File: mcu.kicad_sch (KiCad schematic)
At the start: 8 parts, among them J10 LOLIN-S3 (R), J11 ESP32-S3-DEVKITC-1 (L), J12 ESP32-S3-DEVKITC-1 (R), J13 LOLIN-S2-MINI (L Outer), J14 LOLIN-S2-MINI (R Outer), J15 LOLIN-S2-MINI (L Inner), J16 LOLIN-S2-MINI (R Inner), J9 LOLIN-S3 (L)

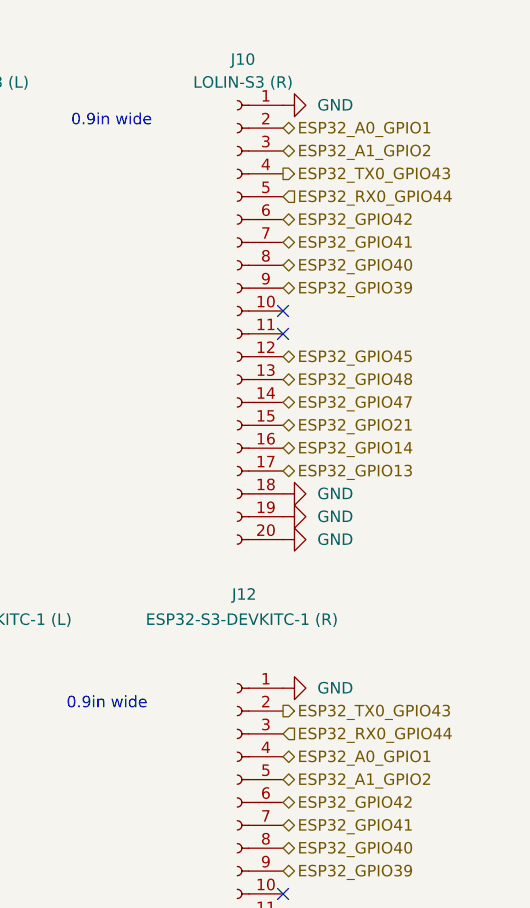
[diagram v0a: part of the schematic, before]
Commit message: Rename UART pins to use Espressif convention
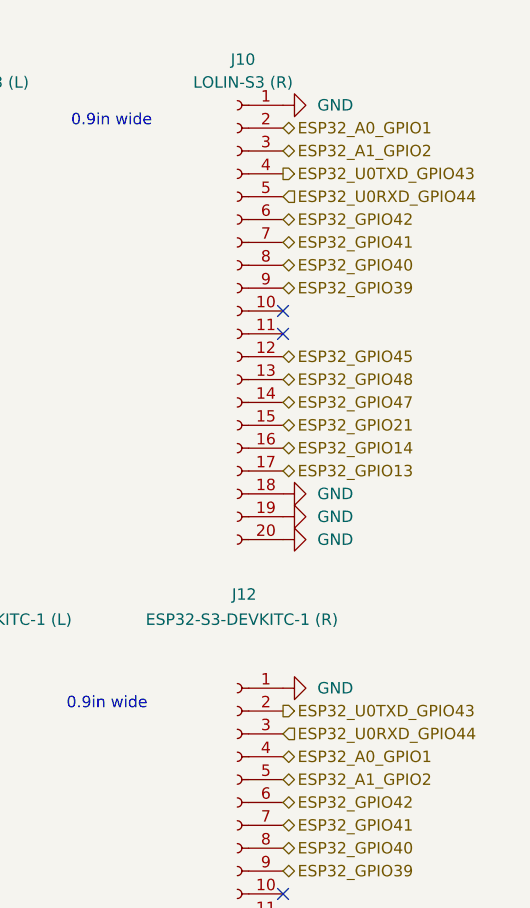
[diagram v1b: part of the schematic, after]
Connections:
- net ESP32_RX0_GPIO44 renamed ESP32_U0RXD_GPIO44
- net ESP32_TX0_GPIO43 renamed ESP32_U0TXD_GPIO43
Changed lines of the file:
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@@
 		)
 	)
-	(hierarchical_label "ESP32_RX0_GPIO44"
+	(hierarchical_label "ESP32_U0RXD_GPIO44"
 		(shape input)
 		(at 69.85 86.36 0)
@@
 		)
 	)
-	(hierarchical_label "ESP32_TX0_GPIO43"
+	(hierarchical_label "ESP32_U0TXD_GPIO43"
 		(shape output)
 		(at 69.85 83.82 0)
@@
 		)
 	)
-	(hierarchical_label "ESP32_TX0_GPIO43"
+	(hierarchical_label "ESP32_U0TXD_GPIO43"
 		(shape output)
 		(at 69.85 24.13 0)
@@
 		)
 	)
-	(hierarchical_label "ESP32_RX0_GPIO44"
+	(hierarchical_label "ESP32_U0RXD_GPIO44"
 		(shape input)
 		(at 69.85 26.67 0)

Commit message: Assign footprints for the remaining components
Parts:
- J10, J9: footprint (none) -> Connector_PinSocket_2.54mm:PinSocket_1x20_P2.54mm_Vertical
- J11, J12: footprint (none) -> Connector_PinHeader_2.54mm:PinHeader_1x22_P2.54mm_Vertical
- J13, J14, J15, J16: footprint (none) -> Connector_PinHeader_2.54mm:PinHeader_1x08_P2.54mm_Vertical
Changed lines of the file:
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@@
 			)
 		)
-		(property "Footprint" ""
+		(property "Footprint" "Connector_PinHeader_2.54mm:PinHeader_1x08_P2.54mm_Vertical"
 			(at 64.77 181.61 0)
 			(effects
@@
 			)
 		)
-		(property "Footprint" ""
+		(property "Footprint" "Connector_PinSocket_2.54mm:PinSocket_1x20_P2.54mm_Vertical"
 			(at 64.77 39.37 0)
 			(effects
@@
 			)
 		)
-		(property "Footprint" ""
+		(property "Footprint" "Connector_PinSocket_2.54mm:PinSocket_1x20_P2.54mm_Vertical"
 			(at 36.83 39.37 0)
 			(effects
@@
 			)
 		)
-		(property "Footprint" ""
+		(property "Footprint" "Connector_PinHeader_2.54mm:PinHeader_1x08_P2.54mm_Vertical"
 			(at 36.83 181.61 0)
 			(effects
@@
 			)
 		)
-		(property "Footprint" ""
+		(property "Footprint" "Connector_PinHeader_2.54mm:PinHeader_1x08_P2.54mm_Vertical"
 			(at 67.31 153.67 0)
 			(effects
@@
 			)
 		)
-		(property "Footprint" ""
+		(property "Footprint" "Connector_PinHeader_2.54mm:PinHeader_1x08_P2.54mm_Vertical"
 			(at 34.29 153.67 0)
 			(effects
@@
 			)
 		)
-		(property "Footprint" ""
+		(property "Footprint" "Connector_PinHeader_2.54mm:PinHeader_1x22_P2.54mm_Vertical"
 			(at 64.77 106.68 0)
 			(effects
@@
 			)
 		)
-		(property "Footprint" ""
+		(property "Footprint" "Connector_PinHeader_2.54mm:PinHeader_1x22_P2.54mm_Vertical"
 			(at 36.83 106.68 0)
 			(effects

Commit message: Place all components
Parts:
- removed J13: LOLIN-S2-MINI (L Outer), Connector_PinHeader_2.54mm:PinHeader_1x08_P2.54mm_Vertical, symbol Connector:Conn_01x08_Socket
- removed J14: LOLIN-S2-MINI (R Outer), Connector_PinHeader_2.54mm:PinHeader_1x08_P2.54mm_Vertical, symbol Connector:Conn_01x08_Socket
- removed J15: LOLIN-S2-MINI (L Inner), Connector_PinHeader_2.54mm:PinHeader_1x08_P2.54mm_Vertical, symbol Connector:Conn_01x08_Socket
- removed J16: LOLIN-S2-MINI (R Inner), Connector_PinHeader_2.54mm:PinHeader_1x08_P2.54mm_Vertical, symbol Connector:Conn_01x08_Socket
- added J13: LOLIN-S2-MINI (L), Connector_PinSocket_2.54mm:PinSocket_2x08_P2.54mm_Vertical, symbol Connector_Generic:Conn_02x08_Odd_Even
- added J14: LOLIN-S2-MINI (R), Connector_PinSocket_2.54mm:PinSocket_2x08_P2.54mm_Vertical, symbol Connector_Generic:Conn_02x08_Odd_Even
- J11, J12: footprint Connector_PinHeader_2.54mm:PinHeader_1x22_P2.54mm_Vertical -> Connector_PinSocket_2.54mm:PinSocket_1x22_P2.54mm_Vertical
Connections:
- net +3.3V: now also J13.16 (Pin_16)
- net +5V: now also J14.15 (Pin_15)
- net ESP32_A0_GPIO1: now also J13.1 (Pin_1)
- net ESP32_A1_GPIO2: now also J13.3 (Pin_3)
- net ESP32_A2_GPIO3: now also J13.4 (Pin_4)
- net ESP32_A3_GPIO4: now also J13.5 (Pin_5)
- net ESP32_A4_GPIO5: now also J13.6 (Pin_6)
- net ESP32_A5_GPIO6: now also J13.7 (Pin_7)
- net ESP32_A6_GPIO7: now also J13.8 (Pin_8)
- net ESP32_A7_GPIO8: now also J13.9 (Pin_9)
- net ESP32_A8_GPIO9: now also J13.10 (Pin_10)
- net ESP32_A9_GPIO10: now also J13.11 (Pin_11)
- net ESP32_GPIO11: now also J13.12 (Pin_12)
- net ESP32_GPIO12: now also J13.14 (Pin_14)
- net ESP32_GPIO13: now also J13.13 (Pin_13)
- net ESP32_GPIO14: now also J13.15 (Pin_15)
- net ESP32_GPIO16: now also J14.11 (Pin_11)
- net ESP32_GPIO17: now also J14.12 (Pin_12)
- net ESP32_GPIO18: now also J14.9 (Pin_9)
- net ESP32_GPIO21: now also J14.10 (Pin_10)
- net ESP32_GPIO33: now also J14.7 (Pin_7)
- net ESP32_GPIO34: now also J14.8 (Pin_8)
- net ESP32_GPIO35: now also J14.5 (Pin_5)
- net ESP32_GPIO36: now also J14.6 (Pin_6)
- net ESP32_GPIO37: now also J14.3 (Pin_3)
- net ESP32_GPIO38: now also J14.4 (Pin_4)
- net ESP32_GPIO39: now also J14.1 (Pin_1)
- net ESP32_GPIO40: now also J14.2 (Pin_2)
- net GND: now also J14.13 (Pin_13), J14.14 (Pin_14)
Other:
- note added: "0.9in wide (outer) 0.7in wide (inner)"
- note removed: "0.7in wide"
- moved on the sheet: J10, J11, J12, J9

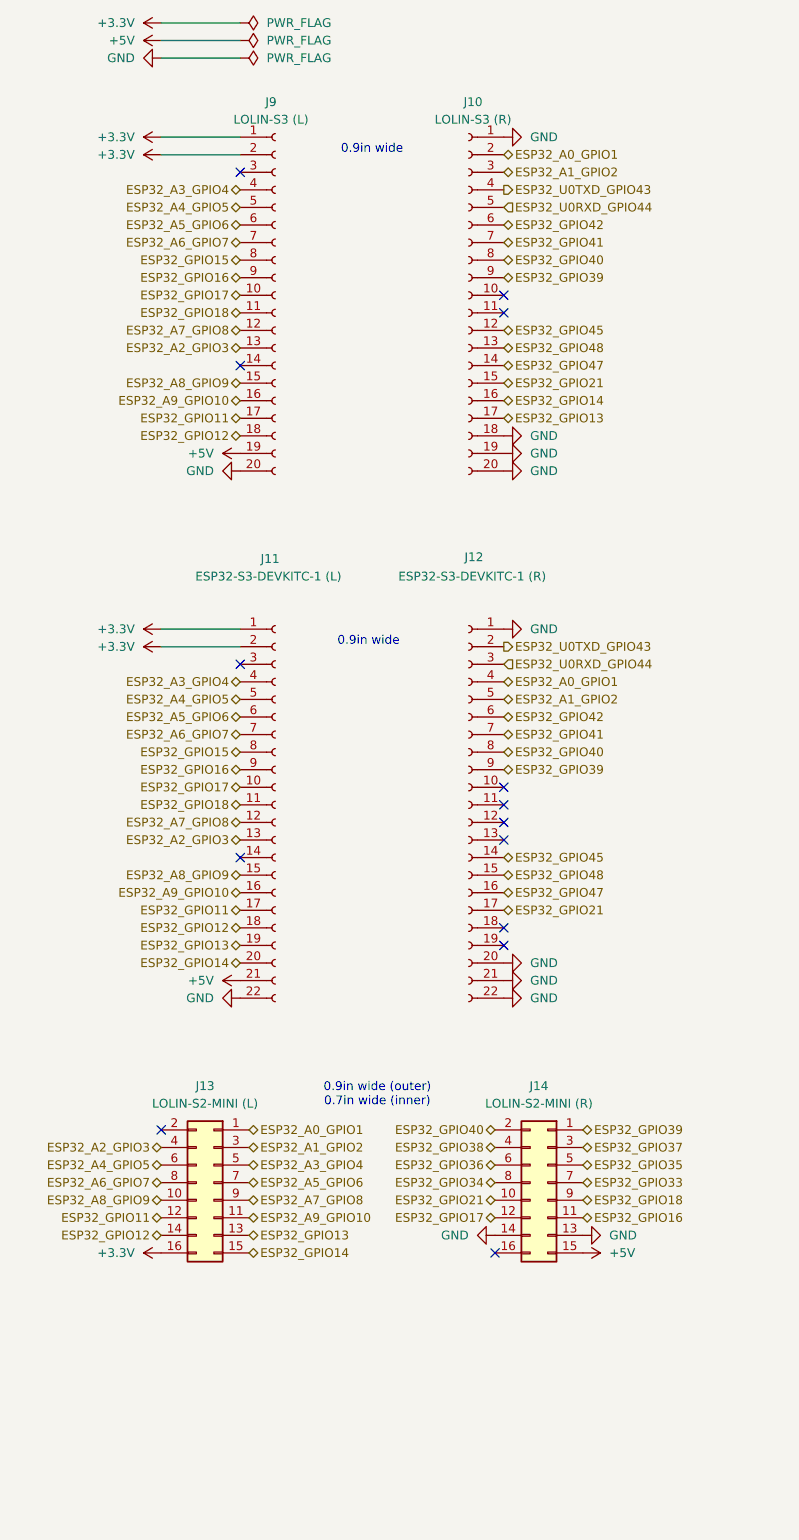
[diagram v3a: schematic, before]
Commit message: Add LOLIN S3 mini support
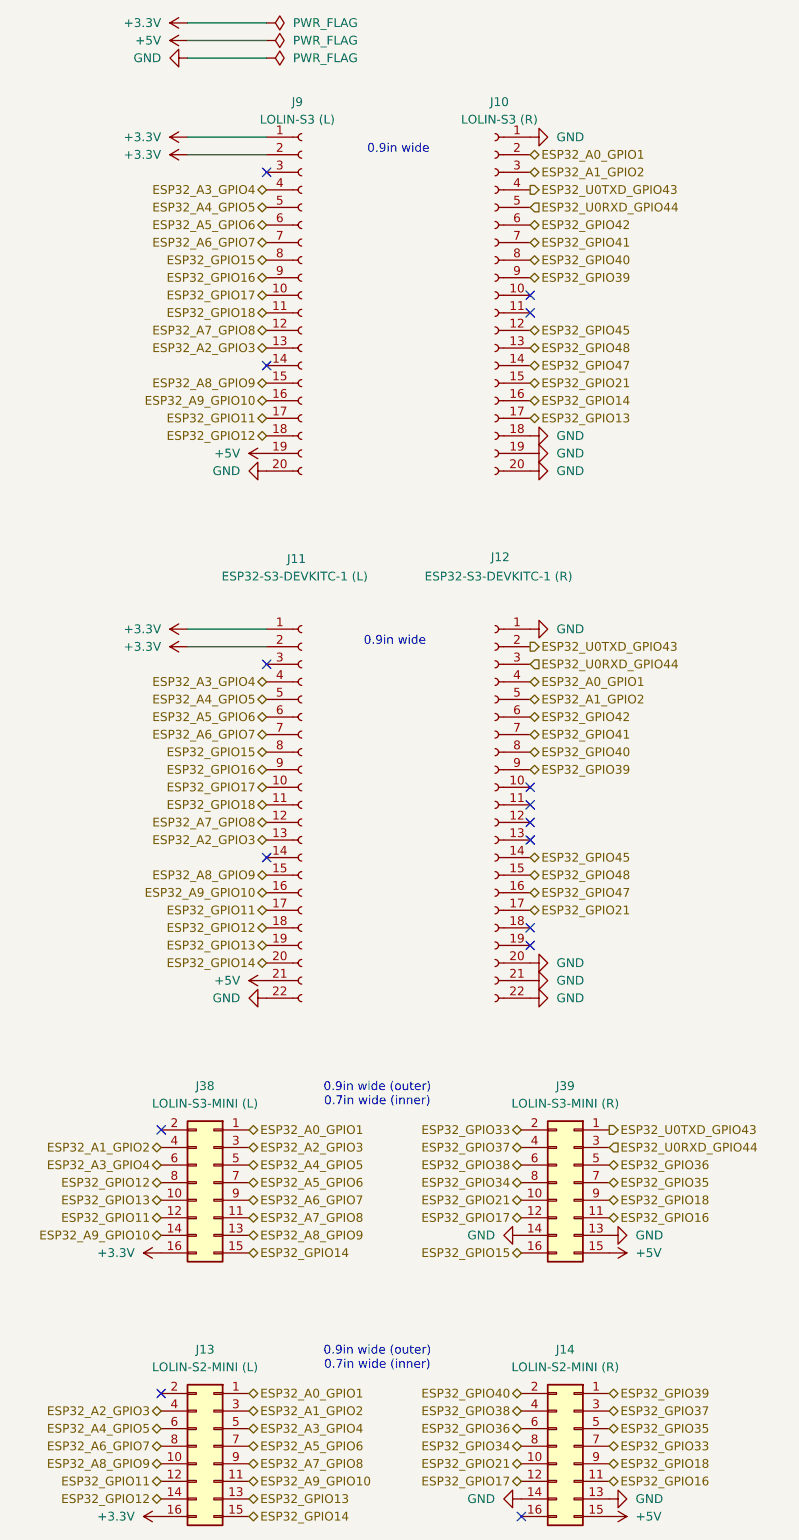
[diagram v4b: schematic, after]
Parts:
- added J13: LOLIN-S2-MINI (L), Connector_PinSocket_2.54mm:PinSocket_2x08_P2.54mm_Vertical, symbol Connector_Generic:Conn_02x08_Odd_Even
- added J14: LOLIN-S2-MINI (R), Connector_PinSocket_2.54mm:PinSocket_2x08_P2.54mm_Vertical, symbol Connector_Generic:Conn_02x08_Odd_Even
- J38: renamed from J13; value LOLIN-S2-MINI (L) -> LOLIN-S3-MINI (L)
- J39: renamed from J14; value LOLIN-S2-MINI (R) -> LOLIN-S3-MINI (R)
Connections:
- net +3.3V: now also J13.16 (Pin_16)
- net +5V: now also J14.15 (Pin_15)
- net ESP32_A0_GPIO1: now also J13.1 (Pin_1)
- net ESP32_A1_GPIO2: now also J38.4 (Pin_4), J13.3 (Pin_3); no longer J38.3 (Pin_3)
- net ESP32_A2_GPIO3: now also J38.3 (Pin_3), J13.4 (Pin_4); no longer J38.4 (Pin_4)
- net ESP32_A3_GPIO4: now also J38.6 (Pin_6), J13.5 (Pin_5); no longer J38.5 (Pin_5)
- net ESP32_A4_GPIO5: now also J38.5 (Pin_5), J13.6 (Pin_6); no longer J38.6 (Pin_6)
- net ESP32_A5_GPIO6: now also J13.7 (Pin_7)
- net ESP32_A6_GPIO7: now also J38.9 (Pin_9), J13.8 (Pin_8); no longer J38.8 (Pin_8)
- net ESP32_A7_GPIO8: now also J38.11 (Pin_11), J13.9 (Pin_9); no longer J38.9 (Pin_9)
- net ESP32_A8_GPIO9: now also J38.13 (Pin_13), J13.10 (Pin_10); no longer J38.10 (Pin_10)
- net ESP32_A9_GPIO10: now also J38.14 (Pin_14), J13.11 (Pin_11); no longer J38.11 (Pin_11)
- net ESP32_GPIO11: now also J13.12 (Pin_12)
- net ESP32_GPIO12: now also J38.8 (Pin_8), J13.14 (Pin_14); no longer J38.14 (Pin_14)
- net ESP32_GPIO13: now also J38.10 (Pin_10), J13.13 (Pin_13); no longer J38.13 (Pin_13)
- net ESP32_GPIO14: now also J13.15 (Pin_15)
- net ESP32_GPIO15: now also J39.16 (Pin_16)
- net ESP32_GPIO16: now also J14.11 (Pin_11)
- net ESP32_GPIO17: now also J14.12 (Pin_12)
- net ESP32_GPIO18: now also J14.9 (Pin_9)
- net ESP32_GPIO21: now also J14.10 (Pin_10)
- net ESP32_GPIO33: now also J39.2 (Pin_2), J14.7 (Pin_7); no longer J39.7 (Pin_7)
- net ESP32_GPIO34: now also J14.8 (Pin_8)
- net ESP32_GPIO35: now also J39.7 (Pin_7), J14.5 (Pin_5); no longer J39.5 (Pin_5)
- net ESP32_GPIO36: now also J39.5 (Pin_5), J14.6 (Pin_6); no longer J39.6 (Pin_6)
- net ESP32_GPIO37: now also J39.4 (Pin_4), J14.3 (Pin_3); no longer J39.3 (Pin_3)
- net ESP32_GPIO38: now also J39.6 (Pin_6), J14.4 (Pin_4); no longer J39.4 (Pin_4)
- net ESP32_GPIO39: now also J14.1 (Pin_1); no longer J39.1 (Pin_1)
- net ESP32_GPIO40: now also J14.2 (Pin_2); no longer J39.2 (Pin_2)
- net ESP32_U0RXD_GPIO44: now also J39.3 (Pin_3)
- net ESP32_U0TXD_GPIO43: now also J39.1 (Pin_1)
- net GND: now also J14.13 (Pin_13), J14.14 (Pin_14)
- no-connect marks 14 -> 15
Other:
- moved on the sheet: J10, J11, J12, J39, J9

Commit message: Renumber references and place LOLIN-S3-MINI
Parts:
- renumbered J9 to J20, J10 to J21, J11 to J22, J12 to J23, J38 to J24, J39 to J25, J13 to J26, J14 to J27
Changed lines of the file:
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@@
 		(on_board yes)
 		(dnp no)
-		(property "Reference" "J39"
+		(property "Reference" "J25"
 			(at 78.74 160.02 0)
 			(effects
@@
 			(project "dali-pcb"
 				(path "/aa7f7e07-1f39-4222-a272-c9975d033b6d/a53b6c42-facd-43a9-ae46-417ca2669247"
-					(reference "J39")
+					(reference "J25")
 					(unit 1)
 				)
@@
 		(dnp no)
 		(fields_autoplaced yes)
-		(property "Reference" "J10"
+		(property "Reference" "J21"
 			(at 69.215 17.78 0)
 			(do_not_autoplace yes)
@@
 			(project "dali-pcb"
 				(path "/aa7f7e07-1f39-4222-a272-c9975d033b6d/a53b6c42-facd-43a9-ae46-417ca2669247"
-					(reference "J10")
+					(reference "J21")
 					(unit 1)
 				)
@@
 		(dnp no)
 		(fields_autoplaced yes)
-		(property "Reference" "J9"
+		(property "Reference" "J20"
 			(at 40.005 17.78 0)
 			(do_not_autoplace yes)
@@
 			(project "dali-pcb"
 				(path "/aa7f7e07-1f39-4222-a272-c9975d033b6d/a53b6c42-facd-43a9-ae46-417ca2669247"
-					(reference "J9")
+					(reference "J20")
 					(unit 1)
 				)
@@
 		(on_board yes)
 		(dnp no)
-		(property "Reference" "J14"
+		(property "Reference" "J27"
 			(at 78.74 198.12 0)
 			(effects
@@
 			(project "dali-pcb"
 				(path "/aa7f7e07-1f39-4222-a272-c9975d033b6d/a53b6c42-facd-43a9-ae46-417ca2669247"
-					(reference "J14")
+					(reference "J27")
 					(unit 1)
 				)
@@
 		(on_board yes)
 		(dnp no)
-		(property "Reference" "J13"
+		(property "Reference" "J26"
 			(at 26.67 198.12 0)
 			(effects
@@
 			(project "dali-pcb"
 				(path "/aa7f7e07-1f39-4222-a272-c9975d033b6d/a53b6c42-facd-43a9-ae46-417ca2669247"
-					(reference "J13")
+					(reference "J26")
 					(unit 1)
 				)
@@
 		(on_board yes)
 		(dnp no)
-		(property "Reference" "J38"
+		(property "Reference" "J24"
 			(at 26.67 160.02 0)
 			(effects
@@
 			(project ""
 				(path "/aa7f7e07-1f39-4222-a272-c9975d033b6d/a53b6c42-facd-43a9-ae46-417ca2669247"
-					(reference "J38")
+					(reference "J24")
 					(unit 1)
 				)
@@
 		(on_board yes)
 		(dnp no)
-		(property "Reference" "J12"
+		(property "Reference" "J23"
 			(at 69.342 83.566 0)
 			(do_not_autoplace yes)
@@
 			(project "dali-pcb"
 				(path "/aa7f7e07-1f39-4222-a272-c9975d033b6d/a53b6c42-facd-43a9-ae46-417ca2669247"
-					(reference "J12")
+					(reference "J23")
 					(unit 1)
 				)
@@
 		(on_board yes)
 		(dnp no)
-		(property "Reference" "J11"
+		(property "Reference" "J22"
 			(at 39.878 83.82 0)
 			(do_not_autoplace yes)
@@
 			(project "dali-pcb"
 				(path "/aa7f7e07-1f39-4222-a272-c9975d033b6d/a53b6c42-facd-43a9-ae46-417ca2669247"
-					(reference "J11")
-					(unit 1)
-				)
+					(reference "J22")
+					(unit 1)
+				)

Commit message: Render PCB
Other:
- moved on the sheet: J20, J21, J22, J23, J24, J25, J26, J27
